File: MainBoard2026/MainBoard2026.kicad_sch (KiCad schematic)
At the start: 73 parts, among them J1 RJ25, J2 RJ25, J3 ICSP, J4 RJ25, J5 GPS_DFROBOT_TEL-0157, J6 Micro_SD_Card_Det_Hirose_DM3AT, J8 BATT_CON, Q4 AO3401A, SW3 POWER, U1 ESP32-WROOM-32, U2 R-78E5.0-0.5, U3 MCP25625-x-SS, U4 BP5293-33, U6 RX8900_mod, Y1 16MHz

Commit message: Add files via upload
AO3401Aのフットプリントを修正
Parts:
- removed Q4: AO3401A, Package_TO_SOT_SMD:SOT-23, symbol Device:Q_PMOS_GDS
- added Q1: AO3401A, Package_TO_SOT_SMD:SOT-23, symbol Transistor_FET:AO3401A
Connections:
- net +BATT: now also Q1.3 (D)
- net at C21.2, D20.1 (K), F2.2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: now also Q1.2 (S)
- net at C21.1, D20.2 (A), R44.2: now also Q1.1 (G)
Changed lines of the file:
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@@
 	(text "G"
 		(exclude_from_sim no)
-		(at 169.926 29.972 0)
+		(at 167.64 23.876 0)
 		(effects
 			(font
@@
 	(text "S"
 		(exclude_from_sim no)
-		(at 163.322 21.844 0)
+		(at 176.276 16.51 0)
 		(effects
 			(font
@@
 	(text "D\n"
 		(exclude_from_sim no)
-		(at 173.736 24.384 0)
+		(at 164.338 16.256 0)
 		(effects
 			(font
@@
 	)
 	(junction
+		(at 157.48 22.86)
+		(diameter 0)
+		(color 0 0 0 0)
+	)
+	(junction
 		(at 196.85 140.97)
 		(diameter 0)
@@
 	)
 	(junction
-		(at 157.48 22.86)
-		(diameter 0)
-		(color 0 0 0 0)
-	)
-	(junction
 		(at 43.18 34.29)
 		(diameter 0)
@@
 	(wire
 		(pts
-			(xy 157.48 22.86) (xy 163.83 22.86)
-		)
-		(stroke
-			(width 0)
-			(type default)
-		)
-	)
-	(wire
-		(pts
 			(xy 196.85 118.11) (xy 198.12 118.11)
 		)
@@
 	(wire
 		(pts
-			(xy 168.91 30.48) (xy 168.91 31.75)
+			(xy 170.18 25.4) (xy 170.18 31.75)
 		)
 		(stroke
@@
 	(wire
 		(pts
-			(xy 173.99 22.86) (xy 185.42 22.86)
+			(xy 26.67 119.38) (xy 26.67 123.19)
 		)
 		(stroke
@@
 	(wire
 		(pts
-			(xy 26.67 119.38) (xy 26.67 123.19)
+			(xy -7.62 187.96) (xy 2.54 187.96)
 		)
 		(stroke
@@
 	(wire
 		(pts
-			(xy -7.62 187.96) (xy 2.54 187.96)
+			(xy 132.08 229.87) (xy 135.89 229.87)
 		)
 		(stroke
@@
 	(wire
 		(pts
-			(xy 132.08 229.87) (xy 135.89 229.87)
+			(xy 262.89 76.2) (xy 262.89 68.58)
 		)
 		(stroke
@@
 	(wire
 		(pts
-			(xy 262.89 76.2) (xy 262.89 68.58)
+			(xy 170.18 31.75) (xy 168.91 31.75)
 		)
 		(stroke
@@
 	(wire
 		(pts
+			(xy 157.48 22.86) (xy 175.26 22.86)
+		)
+		(stroke
+			(width 0)
+			(type default)
+		)
+	)
+	(wire
+		(pts
 			(xy 132.08 229.87) (xy 132.08 279.4)
 		)
@@
 	(wire
 		(pts
+			(xy 175.26 22.86) (xy 175.26 17.78)
+		)
+		(stroke
+			(width 0)
+			(type default)
+		)
+	)
+	(wire
+		(pts
 			(xy 228.6 285.75) (xy 233.68 285.75)
 		)
@@
 	(wire
 		(pts
-			(xy 185.42 12.7) (xy 185.42 22.86)
+			(xy 165.1 12.7) (xy 165.1 17.78)
 		)
 		(stroke
@@
 	)
 	(symbol
+		(lib_id "Transistor_FET:AO3401A")
+		(at 170.18 20.32 90)
+		(unit 1)
+		(exclude_from_sim no)
+		(in_bom yes)
+		(on_board yes)
+		(dnp no)
+		(fields_autoplaced yes)
+		(property "Reference" "Q1"
+			(at 170.18 12.7 90)
+			(effects
+				(font
+					(size 1.27 1.27)
+				)
+			)
+		)
+		(property "Value" "AO3401A"
+			(at 170.18 15.24 90)
+			(effects
+				(font
+					(size 1.27 1.27)
+				)
+			)
+		)
+		(property "Footprint" "Package_TO_SOT_SMD:SOT-23"
+			(at 172.085 15.24 0)
+			(effects
+				(font
+					(size 1.27 1.27)
+					(italic yes)
+				)
+				(justify left)
+				(hide yes)
+			)
+		)
+		(property "Datasheet" "http://www.aosmd.com/pdfs/datasheet/AO3401A.pdf"
+			(at 173.99 15.24 0)
+			(effects
+				(font
+					(size 1.27 1.27)
+				)
+				(justify left)
+				(hide yes)
+			)
+		)
+		(property "Description" "-4.0A Id, -30V Vds, P-Channel MOSFET, SOT-23"
+			(at 170.18 20.32 0)
+			(effects
+				(font
+					(size 1.27 1.27)
+				)
+				(hide yes)
+			)
+		)
+		(pin "1"
+		)
+		(pin "2"
+		)
+		(pin "3"
+		)
+		(instances
+			(project ""
+				(path "/91470f72-cbb4-4917-89df-019a22a28473"
+					(reference "Q1")
+					(unit 1)
+				)
+			)
+		)
+	)
+	(symbol
 		(lib_id "Connector:RJ25")
 		(at -15.24 59.69 0)
@@
 	)
 	(symbol
-		(lib_id "Device:Q_PMOS_GDS")
-		(at 168.91 25.4 270)
-		(mirror x)
-		(unit 1)
-		(exclude_from_sim no)
-		(in_bom yes)
-		(on_board yes)
-		(dnp no)
-		(property "Reference" "Q4"
-			(at 165.1 18.034 90)
-			(effects
-				(font
-					(size 1.27 1.27)
-				)
-				(justify left)
-			)
-		)
-		(property "Value" "AO3401A"
-			(at 165.1 15.494 90)
-			(effects
-				(font
-					(size 1.27 1.27)
-				)
-				(justify left)
-			)
-		)
-		(property "Footprint" "Package_TO_SOT_SMD:SOT-23"
-			(at 171.45 20.32 0)
-			(effects
-				(font
-					(size 1.27 1.27)
-				)
-				(hide yes)
-			)
-		)
-		(property "Datasheet" "~"
-			(at 168.91 25.4 0)
-			(effects
-				(font
-					(size 1.27 1.27)
-				)
-				(hide yes)
-			)
-		)
-		(property "Description" "P-MOSFET transistor, gate/drain/source"
-			(at 168.91 25.4 0)
-			(effects
-				(font
-					(size 1.27 1.27)
-				)
-				(hide yes)
-			)
-		)
-		(pin "3"
-		)
-		(pin "2"
-		)
-		(pin "1"
-		)
-		(instances
-			(project "MainBoard2026"
-				(path "/91470f72-cbb4-4917-89df-019a22a28473"
-					(reference "Q4")
-					(unit 1)
-				)
-			)
-		)
-	)
-	(symbol
 		(lib_id "Device:C")
 		(at 57.15 187.96 90)
@@
 		(dnp no)
 		(property "Reference" "R3"
-			(at 180.594 276.098 90)
+			(at 181.61 274.066 90)
 			(effects
 				(font
@@
 		)
 		(property "Value" "10k"
-			(at 180.34 274.32 90)
+			(at 181.61 275.844 90)
 			(effects
 				(font
@@
 	(symbol
 		(lib_id "power:+BATT")
-		(at 185.42 12.7 0)
+		(at 165.1 12.7 0)
 		(unit 1)
 		(exclude_from_sim no)
@@
 		(on_board yes)
 		(dnp no)
-		(fields_autoplaced yes)
 		(property "Reference" "#PWR047"
-			(at 185.42 16.51 0)
+			(at 165.1 16.51 0)
 			(effects
 				(font
@@
 		)
 		(property "Value" "+BATT"
-			(at 187.96 11.4299 0)
+			(at 162.306 8.89 0)
 			(effects
 				(font
@@
 		)
 		(property "Footprint" ""
-			(at 185.42 12.7 0)
+			(at 165.1 12.7 0)
 			(effects
 				(font
@@
 		)
 		(property "Datasheet" ""
-			(at 185.42 12.7 0)
+			(at 165.1 12.7 0)
 			(effects
 				(font
@@
 		)
 		(property "Description" "Power symbol creates a global label with name \"+BATT\""
-			(at 185.42 12.7 0)
+			(at 165.1 12.7 0)
 			(effects
 				(font

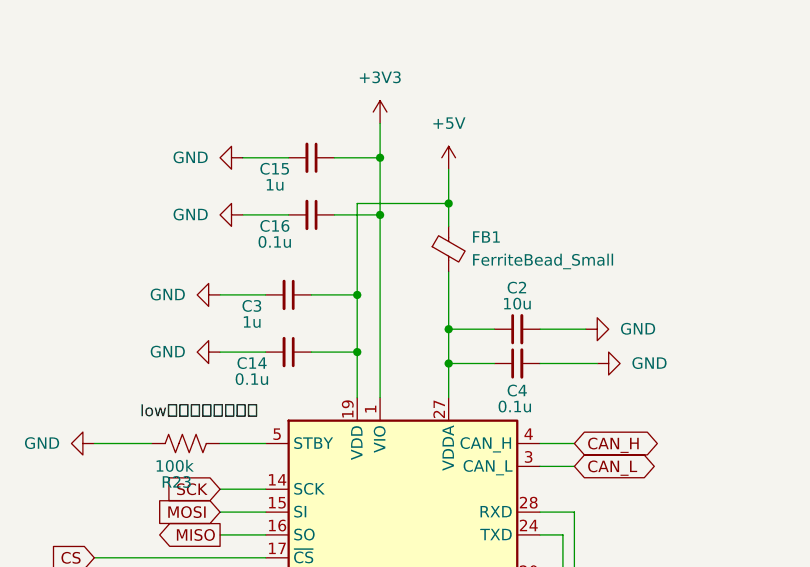
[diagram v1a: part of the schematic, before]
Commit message: Add files via upload
MCP25625のピン19を3V3に変更
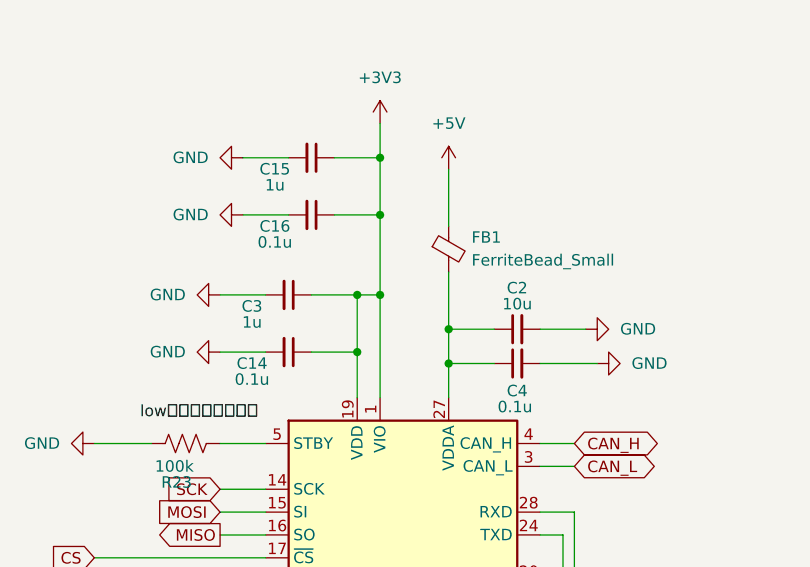
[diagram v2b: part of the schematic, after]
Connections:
- net +3V3: now also C14.1, C3.1, U3.19 (VDD)
- net +5V: no longer C14.1, C3.1, U3.19 (VDD)
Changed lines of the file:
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@@
+	)
+	(junction
+		(at 200.66 237.49)
+		(diameter 0)
+		(color 0 0 0 0)
 	)
 	(junction
@@
 	)
 	(junction
-		(at 208.28 227.33)
-		(diameter 0)
-		(color 0 0 0 0)
-	)
-	(junction
 		(at 168.91 48.26)
 		(diameter 0)
@@
 	)
 	(junction
+		(at 198.12 237.49)
+		(diameter 0)
+		(color 0 0 0 0)
+	)
+	(junction
 		(at 43.18 34.29)
 		(diameter 0)
@@
 	(junction
 		(at 208.28 245.11)
-		(diameter 0)
-		(color 0 0 0 0)
-	)
-	(junction
-		(at 198.12 237.49)
 		(diameter 0)
 		(color 0 0 0 0)
@@
 	(wire
 		(pts
-			(xy 198.12 227.33) (xy 208.28 227.33)
-		)
-		(stroke
-			(width 0)
-			(type default)
-		)
-	)
-	(wire
-		(pts
 			(xy 26.67 119.38) (xy 26.67 123.19)
 		)
@@
 	(wire
 		(pts
-			(xy 208.28 223.52) (xy 208.28 227.33)
-		)
-		(stroke
-			(width 0)
-			(type default)
-		)
-	)
-	(wire
-		(pts
 			(xy 78.74 251.46) (xy 83.82 251.46)
 		)
@@
 	(wire
 		(pts
-			(xy 200.66 228.6) (xy 200.66 248.92)
+			(xy 200.66 228.6) (xy 200.66 237.49)
 		)
 		(stroke
@@
 	(wire
 		(pts
-			(xy 208.28 227.33) (xy 208.28 229.87)
+			(xy 208.28 223.52) (xy 208.28 229.87)
 		)
 		(stroke
@@
 	(wire
 		(pts
-			(xy 198.12 227.33) (xy 198.12 237.49)
-		)
-		(stroke
-			(width 0)
-			(type default)
-		)
-	)
-	(wire
-		(pts
 			(xy 120.65 156.21) (xy 129.54 156.21)
 		)
@@
 	(wire
 		(pts
+			(xy 198.12 237.49) (xy 200.66 237.49)
+		)
+		(stroke
+			(width 0)
+			(type default)
+		)
+	)
+	(wire
+		(pts
 			(xy 180.34 135.89) (xy 187.96 135.89)
 		)
@@
 		)
 		(stroke
+			(width 0)
+			(type default)
+		)
+	)
+	(wire
+		(pts
+			(xy 200.66 237.49) (xy 200.66 248.92)
+		)
+		(stroke
